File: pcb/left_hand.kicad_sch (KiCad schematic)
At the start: 1 part

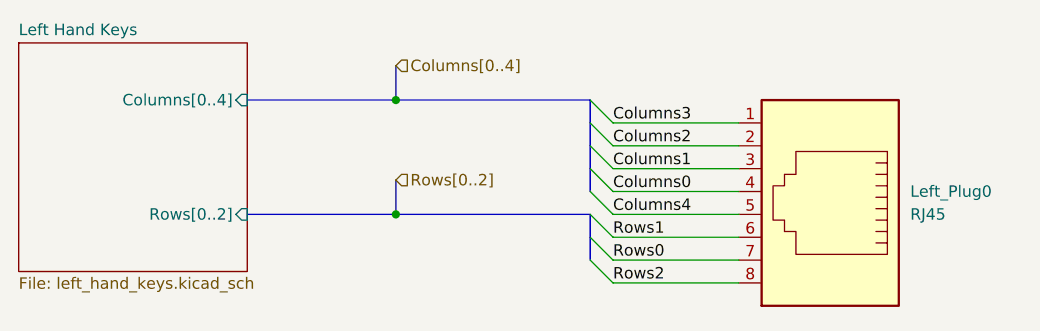
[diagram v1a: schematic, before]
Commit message: Add DNP for right hand
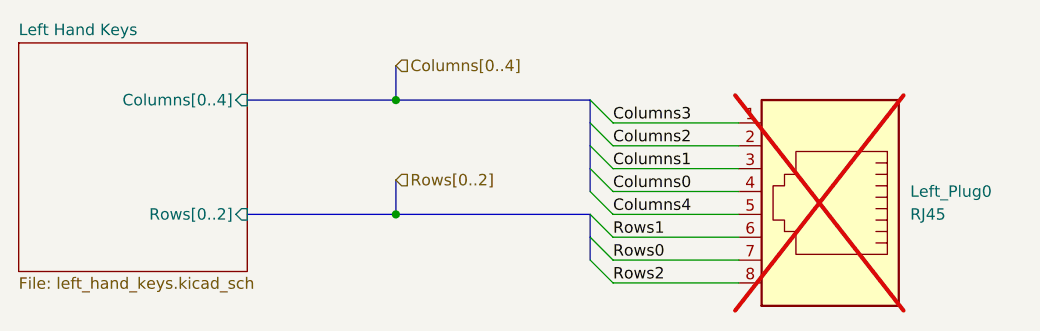
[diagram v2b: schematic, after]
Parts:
- Left_Plug0: now not fitted
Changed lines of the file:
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@@
 		(in_bom yes)
 		(on_board yes)
-		(dnp no)
+		(dnp yes)
 		(fields_autoplaced yes)
 		(property "Reference" "Left_Plug0"
